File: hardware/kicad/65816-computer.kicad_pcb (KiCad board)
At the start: 4 copper layers, 169.5 x 99.7 mm, 61 parts, among them J1 Ext_Pwr_Led, J2 Ext_Sw_Res, J3 Power, J4 UART_A, J5 UART_B, J6 Port_A, J7 Port_B, SW1 SW_Res, U1 74AC04, U11 74AC138, U12 SC16C752, U13 W65C22S, U2 74AC245, U3 74AC573, U4 W65C816S, U5 DS1813-5+, U6 Address_Decoder, U7 AS6C4008, U8 AS6C4008, U9 AT28C256, X1 MXO45HS

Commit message: update schematic, add draft PCB
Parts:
- removed the REF** at (-217.2, 150.5)
- removed the REF** at (-148.0, 147.3)
- removed the REF** at (-155.6, 231.8)
- removed the REF** at (-194.3, 231.8)
- removed the REF** at (-170.8, 238.8)
- removed the REF** at (-155.6, 238.8)
- removed the REF** at (-215.9, 226.1)
- removed the REF** at (-147.3, 238.1)
- removed the REF** at (-292.1, 203.2)
- removed the REF** at (-158.1, 238.8)
- removed the REF** at (-308.6, 238.1)
- removed the REF** at (-165.7, 238.8)
- removed the REF** at (-163.2, 238.8)
- removed the REF** at (-173.4, 239.0)
- removed the REF** at (-308.6, 147.3)
- removed the REF** at (-155.6, 234.3)
- removed the REF** at (-168.3, 238.8)
- removed the REF** at (-160.7, 238.8)
- added C13: 0.1 µF, Capacitor_SMD:C_0603_1608Metric_Pad1.08x0.95mm_HandSolder, F.Cu at (147.3, 97.2)
- added C14: 0.1 µF, Capacitor_SMD:C_0603_1608Metric_Pad1.08x0.95mm_HandSolder, F.Cu at (170.8, 62.5)
- added C15: C_Polarized, Capacitor_THT:CP_Radial_D6.3mm_P2.50mm, F.Cu at (126.1, 45.0)
- added H1: MountingHole_Pad, MountingHole:MountingHole_3.2mm_M3_Pad_Via, F.Cu at (73.5, 44.8)
- added H2: MountingHole_Pad, MountingHole:MountingHole_3.2mm_M3_Pad_Via, F.Cu at (232.8, 45.0)
- added H3: MountingHole_Pad, MountingHole:MountingHole_3.2mm_M3_Pad_Via, F.Cu at (73.5, 134.2)
- added H4: MountingHole_Pad, MountingHole:MountingHole_3.2mm_M3_Pad_Via, F.Cu at (232.9, 134.4)
- added J10: Conn_01x08, Connector_PinHeader_2.54mm:PinHeader_1x08_P2.54mm_Vertical, F.Cu at (201.9, 126.7)
- added J11: Conn_01x04, Connector_PinHeader_2.54mm:PinHeader_1x04_P2.54mm_Vertical, F.Cu at (146.1, 44.5)
- added J12: Conn_01x08, Connector_PinHeader_2.54mm:PinHeader_1x08_P2.54mm_Vertical, F.Cu at (80.8, 87.9)
- added J8: Conn_01x08, Connector_PinHeader_2.54mm:PinHeader_1x08_P2.54mm_Vertical, F.Cu at (201.9, 133.6)
- added J9: Conn_01x08, Connector_PinHeader_2.54mm:PinHeader_1x08_P2.54mm_Vertical, F.Cu at (227.1, 133.6)
- added JP2: CLK_SEL, Connector_PinHeader_2.54mm:PinHeader_1x03_P2.54mm_Vertical, F.Cu at (115.0, 44.5)
- added JP3: Jumper_2_Bridged, Connector_PinHeader_2.54mm:PinHeader_1x02_P2.54mm_Vertical, F.Cu at (112.0, 70.6)
- added R10: 10 k, Resistor_SMD:R_0603_1608Metric_Pad0.98x0.95mm_HandSolder, F.Cu at (219.5, 127.5)
- added R11: 10 k, Resistor_SMD:R_0603_1608Metric_Pad0.98x0.95mm_HandSolder, F.Cu at (216.9, 127.5)
- added R12: 10 k, Resistor_SMD:R_0603_1608Metric_Pad0.98x0.95mm_HandSolder, F.Cu at (214.4, 127.5)
- added R13: 10 k, Resistor_SMD:R_0603_1608Metric_Pad0.98x0.95mm_HandSolder, F.Cu at (211.8, 127.5)
- added R14: 10 k, Resistor_SMD:R_0603_1608Metric_Pad0.98x0.95mm_HandSolder, F.Cu at (209.3, 127.5)
- added R15: 10 k, Resistor_SMD:R_0603_1608Metric_Pad0.98x0.95mm_HandSolder, F.Cu at (188.6, 81.3)
- added R16: 10 k, Resistor_SMD:R_0603_1608Metric_Pad0.98x0.95mm_HandSolder, F.Cu at (186.7, 81.3)
- added R7: 10 k, Resistor_SMD:R_0603_1608Metric_Pad0.98x0.95mm_HandSolder, F.Cu at (227.1, 127.5)
- added R8: 10 k, Resistor_SMD:R_0603_1608Metric_Pad0.98x0.95mm_HandSolder, F.Cu at (224.5, 127.5)
- added R9: 10 k, Resistor_SMD:R_0603_1608Metric_Pad0.98x0.95mm_HandSolder, F.Cu at (222.0, 127.5)
- added REF**: Oscillator_SMD_IDT_JU6-6_7.0x5.0mm_P2.54mm, Oscillator:Oscillator_SMD_IDT_JU6-6_7.0x5.0mm_P2.54mm, F.Cu at (93.5, 60.9)
- added SW2: SW_DIP_x02, Button_Switch_SMD:SW_DIP_SPSTx02_Slide_6.7x6.64mm_W8.61mm_P2.54mm_LowProfile, F.Cu at (185.4, 90.9)
- added TP1: CLK, TestPoint:TestPoint_Keystone_5005-5009_Compact, F.Cu at (119.4, 72.4)
- added TP10: GND, TestPoint:TestPoint_Keystone_5005-5009_Compact, F.Cu at (182.2, 79.4)
- added TP11: X1_OUT, TestPoint:TestPoint_Keystone_5005-5009_Compact, F.Cu at (123.7, 51.1)
- added TP2: X2_OUT, TestPoint:TestPoint_Keystone_5005-5009_Compact, F.Cu at (117.6, 51.1)
- added TP3: RES, TestPoint:TestPoint_Pad_D1.5mm, F.Cu at (83.3, 118.9)
- added TP4: ~{RES}, TestPoint:TestPoint_Keystone_5005-5009_Compact, F.Cu at (113.0, 99.1)
- added TP7: GND, TestPoint:TestPoint_Keystone_5005-5009_Compact, F.Cu at (124.5, 72.4)
- added TP8: GND, TestPoint:TestPoint_Keystone_5005-5009_Compact, F.Cu at (184.8, 111.8)
- added TP9: GND, TestPoint:TestPoint_Keystone_5005-5009_Compact, F.Cu at (118.1, 99.3)
- added U10: 74AC74, Package_DIP:DIP-14_W7.62mm_Socket, F.Cu at (105.4, 64.6)
- added X2: MXO45HS, Oscillator:Oscillator_DIP-8, F.Cu at (73.8, 64.8)
- J1: value Ext_Pwr_Led -> EXT_LED_PWR
- J2: value Ext_Sw_Res -> EXT_SW_RES
- J3: footprint Connector_PinHeader_2.54mm:PinHeader_1x02_P2.54mm_Vertical -> Connector_JST:JST_XH_B2B-XH-A_1x02_P2.50mm_Vertical
- R4, R5, R6: value 1k -> 1 k
- SW1: value SW_Res -> SW_RES
- U1: value 74AC04 -> SST39LF010; footprint Package_DIP:DIP-14_W7.62mm_Socket -> Package_LCC:PLCC-32_11.4x14.0mm_P1.27mm
- U5: value DS1813-5+ -> MIC2775; footprint Package_TO_SOT_THT:TO-92 -> Package_TO_SOT_SMD:SOT-23-5_HandSoldering
- moved C5 534.0 mm to (176.8, 122.4), turned to 180 degrees
- moved R6 517.0 mm to (105.9, 47.9), turned to 180 degrees
- moved R3 494.2 mm to (137.2, 97.2), turned to -90 degrees
- moved C4 493.8 mm to (139.7, 51.7), turned to 180 degrees
- moved C3 493.3 mm to (139.7, 64.5), turned to 180 degrees
- moved C9 475.4 mm to (195.0, 102.1)
- moved U1 463.8 mm to (184.2, 62.9), turned to 90 degrees
- moved R2 436.7 mm to (132.1, 97.2), turned to -90 degrees
- moved C8 412.9 mm to (93.7, 125.5), turned to -90 degrees
- moved C10 406.2 mm to (190.5, 81.3), turned to -90 degrees
- moved X1 404.3 mm to (89.7, 64.6)
- moved J3 399.2 mm to (84.6, 46.0)
- moved C2 398.5 mm to (200.6, 51.8)
- moved C6 397.0 mm to (72.9, 53.1), turned to 180 degrees
- moved C7 396.7 mm to (79.5, 71.6)
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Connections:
- J2 pad 1: /CPU& Bank Address Latching/~{RES} -> /CPU& Bank Address Latching/~{RES_BTN}
- J4 pad 8: /IO/UART_TXA -> /IO/UART_RXA
- SW1 pad 1: /CPU& Bank Address Latching/~{RES} -> GND
- SW1 pad 2: GND -> /CPU& Bank Address Latching/~{RES_BTN}
- U1 pad 1: /CPU& Bank Address Latching/CLK -> GND
- U1 pad 10: unconnected-(U1-Pad10) -> /CPU& Bank Address Latching/A2
- U1 pad 11: GND -> /CPU& Bank Address Latching/A1
- U1 pad 12: unconnected-(U1-Pad12) -> /CPU& Bank Address Latching/A0
- U1 pad 13: GND -> /CPU& Bank Address Latching/D0
- U1 pad 14: +5V -> /CPU& Bank Address Latching/D1
- U1 pad 2: /CPU& Bank Address Latching/CLK_INV -> GND
- U1 pad 3: /CPU& Bank Address Latching/~{RES} -> GND
- U1 pad 4: /CPU& Bank Address Latching/RES -> /CPU& Bank Address Latching/A12
- U1 pad 5: GND -> /CPU& Bank Address Latching/A7
- U1 pad 6: unconnected-(U1-Pad6) -> /CPU& Bank Address Latching/A6
- U1 pad 7: GND -> /CPU& Bank Address Latching/A5
- U1 pad 8: unconnected-(U1-Pad8) -> /CPU& Bank Address Latching/A4
- U1 pad 9: GND -> /CPU& Bank Address Latching/A3
- U11 pad 10: unconnected-(U11-Pad10) -> /IO/~{IO5}
- U11 pad 11: unconnected-(U11-Pad11) -> /IO/~{IO4}
- U11 pad 12: unconnected-(U11-Pad12) -> /IO/~{IO3}
- U11 pad 7: unconnected-(U11-Pad7) -> /IO/~{IO7}
- U11 pad 9: unconnected-(U11-Pad9) -> /IO/~{IO6}
- U12 pad 13: /CPU& Bank Address Latching/CLK -> /CPU& Bank Address Latching/CLK_UART
- U12 pad 17: unconnected-(U12-Pad17) -> GND
- U12 pad 42: unconnected-(U12-Pad42) -> +5V
- U12 pad 5: /IO/UART_TXA -> /IO/UART_RXA
- U13 pad 23: /IO/~{IOCS} -> /IO/~{IO0}
- U4 pad 39: unconnected-(U4-Pad39) -> /CPU& Bank Address Latching/VDA
- U4 pad 7: unconnected-(U4-Pad7) -> /CPU& Bank Address Latching/VPA
- U5 pad 2: +5V -> GND
- U5 pad 3: GND -> /CPU& Bank Address Latching/RES
- U6 pad 13: unconnected-(U6-Pad13) -> Net-(U6-Pad13)
- U6 pad 3: unconnected-(U6-Pad3) -> /CPU& Bank Address Latching/VPA
- U6 pad 4: unconnected-(U6-Pad4) -> /CPU& Bank Address Latching/VDA
- U9 pad 1: GND -> /Memory/ROMSW1
- U9 pad 26: GND -> /Memory/ROMSW0
- X1 pad 1: unconnected-(X1-Pad1) -> +5V
- X1 pad 5: /CPU& Bank Address Latching/CLK -> /CPU& Bank Address Latching/CLK_UART
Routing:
- net /CPU& Bank Address Latching/A0: track 51.9 -> 354.6 mm, vias 0 -> 2
- net /CPU& Bank Address Latching/A1: track 51.6 -> 347.6 mm, vias 0 -> 2
- net /CPU& Bank Address Latching/A2: track 51.8 -> 342.4 mm, vias 0 -> 2
- net /CPU& Bank Address Latching/A18: track 25.8 -> 302.0 mm
- net /Memory/~{RAM1CS}: track 0.00 -> 272.6 mm, vias 0 -> 3
- net /CPU& Bank Address Latching/A17: track 25.7 -> 283.8 mm
- net /CPU& Bank Address Latching/A16: track 25.9 -> 283.1 mm
- net /CPU& Bank Address Latching/RES: track 0.00 -> 257.0 mm, vias 0 -> 3
- net /CPU& Bank Address Latching/A10: track 51.5 -> 301.1 mm, vias 0 -> 1
- net /Memory/~{RD}: track 51.6 -> 288.3 mm, vias 0 -> 1
- net /CPU& Bank Address Latching/A11: track 51.6 -> 286.0 mm, vias 0 -> 1
- net /CPU& Bank Address Latching/A9: track 51.5 -> 264.6 mm, vias 0 -> 1
- net /CPU& Bank Address Latching/A12: track 51.5 -> 258.8 mm, vias 0 -> 1
- net /Memory/~{WR}: track 25.8 -> 226.0 mm, vias 0 -> 1
- net /CPU& Bank Address Latching/D4: track 158.7 -> 357.9 mm, vias 0 -> 1
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- added copper zone on In1.Cu, net +5V
- added copper zone on In2.Cu, net GND
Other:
- board size 169.5 x 99.7 mm -> 169.7 x 99.8 mm
- board text added: "(c) 2022 Michael Billington"
- board text added: "A0"
- board text added: "A1"
- board text added: "A10"
- board text added: "A11"
- board text added: "A12"
- board text added: "A13"
- board text added: "A14"
- board text added: "A15"
- board text added: "A16"
- board text added: "A17"
- board text added: "A18"
- board text added: "A19"
- board text added: "A2"
- board text added: "A3"
- board text added: "A4"
- board text added: "A5"
- board text added: "A6"
- board text added: "A7"
- board text added: "A8"
- board text added: "A9"
- board text added: "D0"
- board text added: "D1"
- board text added: "D2"
- board text added: "D3"
- board text added: "D4"
- board text added: "D5"
- board text added: "D6"
- board text added: "D7"
- board text added: "GND"
- board text added: "OUT"
- board text added: "PWR"
- board text added: "RES"
- board text added: "RESET"
- board text added: "X1"
- board text added: "X2"
- board text added: "~{CE}"
- board text added: "~{OE}"
- board text added: "~{WE}"

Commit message: pcb updates
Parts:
- added C16: 4.7 µF, Capacitor_THT:CP_Radial_D4.0mm_P1.50mm, F.Cu at (130.7, 125.9)
- added D3: EMU, LED_SMD:LED_0603_1608Metric_Pad1.05x0.95mm_HandSolder, F.Cu at (163.1, 42.9)
- added J13: Conn_01x06, Connector_PinHeader_2.54mm:PinHeader_1x06_P2.54mm_Vertical, F.Cu at (135.1, 69.3)
- added J14: Conn_01x06, Connector_PinHeader_2.54mm:PinHeader_1x06_P2.54mm_Vertical, F.Cu at (117.2, 93.3)
- added J15: Conn_01x02, Connector_PinHeader_2.54mm:PinHeader_1x02_P2.54mm_Vertical, F.Cu at (79.5, 135.4)
- added J16: Conn_01x06, Connector_PinHeader_2.54mm:PinHeader_1x06_P2.54mm_Vertical, F.Cu at (98.3, 72.1)
- added J17: Conn_01x04, Connector_PinHeader_2.54mm:PinHeader_1x04_P2.54mm_Vertical, F.Cu at (80.8, 71.9)
- added J18: Conn_01x07, Connector_PinSocket_2.54mm:PinSocket_1x07_P2.54mm_Vertical, F.Cu at (111.5, 126.0)
- added J19: Conn_02x06, Connector_PinHeader_2.54mm:PinHeader_2x03_P2.54mm_Vertical, F.Cu at (132.2, 135.0)
- added J20: Conn_01x02, Connector_PinHeader_2.54mm:PinHeader_1x02_P2.54mm_Vertical, F.Cu at (187.3, 119.1)
- added JP4: Jumper_2_Bridged, Connector_PinHeader_2.54mm:PinHeader_1x02_P2.54mm_Vertical, F.Cu at (106.8, 92.4)
- added JP5: SolderJumper_2_Open, Jumper:SolderJumper-2_P1.3mm_Open_RoundedPad1.0x1.5mm, F.Cu at (140.1, 44.3)
- added R17: 1 k, Resistor_SMD:R_0603_1608Metric_Pad0.98x0.95mm_HandSolder, F.Cu at (167.8, 42.9)
- added TP5: ~{IRQ}, TestPoint:TestPoint_Keystone_5005-5009_Compact, F.Cu at (108.2, 99.1)
- added TP6: ~{NMI}, TestPoint:TestPoint_Keystone_5005-5009_Compact, F.Cu at (183.1, 104.5)
- added U14: DS1813-5+, Package_TO_SOT_THT:TO-92_Inline, F.Cu at (133.2, 44.6)
- added X2_ALT: Oscillator_SMD_IDT_JU6-6_7.0x5.0mm_P2.54mm, Oscillator:Oscillator_SMD_IDT_JU6-6_7.0x5.0mm_P2.54mm, F.Cu at (77.6, 61.0)
- C15: value C_Polarized -> 100 µF
- U13, U4: footprint Package_DIP:DIP-40_W15.24mm -> Package_DIP:DIP-40_W15.24mm_Socket
- moved R3 22.4 mm to (122.0, 80.6), turned to 0 degrees
- moved J4 19.2 mm to (101.6, 132.8), turned to -90 degrees
- moved R1 17.0 mm to (122.0, 85.7), turned to 0 degrees
- moved J7 16.4 mm to (162.2, 134.9)
- moved J6 16.4 mm to (142.4, 134.9)
- moved R2 11.9 mm to (122.0, 90.8), turned to 0 degrees
- moved JP1 9.71 mm to (125.7, 119.5)
- moved TP3 8.29 mm to (87.1, 126.2)
- moved TP8 8.18 mm to (188.3, 104.4)
- moved C7 6.53 mm to (75.4, 76.7), turned to -90 degrees
- moved LS1 5.77 mm to (118.2, 111.9), turned to 180 degrees
- moved JP2 5.06 mm to (120.0, 44.5), turned to -90 degrees
- moved TP2 3.72 mm to (113.9, 50.5)
- moved JP3 3.18 mm to (109.2, 72.1), turned to -90 degrees
- moved C5 1.73 mm to (178.1, 123.6), turned to -90 degrees
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- renumbered REF** to X1_ALT
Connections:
- net Net-(JP1-Pad2) renamed /IO/SPEAKER
- net Net-(U6-Pad13) renamed /Memory/S0
- U12 pad 29: unconnected-(U12-Pad29) -> /IO/UART_INTB
- U12 pad 30: unconnected-(U12-Pad30) -> /IO/UART_INTA
- U4 pad 1: unconnected-(U4-Pad1) -> /CPU& Bank Address Latching/~{VP}
- U4 pad 35: unconnected-(U4-Pad35) -> /CPU& Bank Address Latching/EMU
- U4 pad 38: unconnected-(U4-Pad38) -> /CPU& Bank Address Latching/MX
- U4 pad 4: +5V -> /CPU& Bank Address Latching/~{IRQ}
- U4 pad 5: unconnected-(U4-Pad5) -> /CPU& Bank Address Latching/~{ML}
- U6 pad 20: unconnected-(U6-Pad20) -> /Memory/S1
- U6 pad 21: unconnected-(U6-Pad21) -> /Memory/S2
- U6 pad 22: unconnected-(U6-Pad22) -> /Memory/S3
- U6 pad 23: unconnected-(U6-Pad23) -> /Memory/S4
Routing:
- net /CPU& Bank Address Latching/~{RES}: track 148.7 -> 225.5 mm, vias 3 -> 2
- net /CPU& Bank Address Latching/EMU: track 0.00 -> 63.0 mm
- net /CPU& Bank Address Latching/~{IRQ}: track 0.00 -> 44.5 mm
- net /IO/VIA_PB7: track 63.7 -> 104.7 mm, vias 1 -> 0
- net /IO/~{UART_TXRDYA}: track 17.0 -> 52.4 mm
- net /CPU& Bank Address Latching/~{NMI}: track 61.4 -> 93.5 mm, vias 2 -> 3
- net /IO/UART_INTA: track 0.00 -> 30.1 mm
- net /Memory/~{WR}: track 226.0 -> 256.0 mm
- net /CPU& Bank Address Latching/~{ML}: track 0.00 -> 29.5 mm
- net /IO/UART_INTB: track 0.00 -> 27.9 mm
- net /IO/VIA_PA0: track 16.3 -> 43.1 mm
- net /IO/VIA_PA1: track 12.3 -> 38.4 mm
- net /IO/~{UART_RIA}: track 16.8 -> 41.9 mm
- net /IO/VIA_PA2: track 15.8 -> 39.6 mm
- net /IO/~{UART_CDA}: track 14.2 -> 36.3 mm
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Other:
- board text added: "+"
- board text added: "1.8432 MHz"
- board text added: "65C816"
- board text added: "74AC138"
- board text added: "74AC245"
- board text added: "74AC573"
- board text added: "74AC74"
- board text added: "AS6C4008"
- board text added: "AT28C256"
- board text added: "ATF22V10 Address Decode"
- board text added: "BE"
- board text added: "CA1"
- board text added: "CA2"
- board text added: "CB1"
- board text added: "CB2"
- board text added: "CLK"
- board text added: "CPU"
- board text added: "CS1"
- board text added: "EMU"
- board text added: "INTA"
- board text added: "INTB"
- board text added: "MX"
- board text added: "NC"
- board text added: "PA0"
- board text added: "PA1"
- board text added: "PA2"
- board text added: "PA3"
- board text added: "PA4"
- board text added: "PA5"
- board text added: "PA6"
- board text added: "PA7"
- board text added: "PB0"
- board text added: "PB1"
- board text added: "PB2"
- board text added: "PB3"
- board text added: "PB4"
- board text added: "PB5"
- board text added: "PB6"
- board text added: "PB7"
- board text added: "RAM0"
- board text added: "RAM1"
- board text added: "ROM"
- board text added: "ROM_BANK"
- board text added: "RX"
- board text added: "R~{W}"
- board text added: "S0"
- board text added: "S1"
- board text added: "S2"
- board text added: "S3"
- board text added: "S4"
- board text added: "SEL"
- board text added: "SPEAKER"
- board text added: "SST39LF010 ROM"
- board text added: "TX"
- board text added: "T~{R}"
- board text added: "U14_ENABLE"
- board text added: "VCC"
- board text added: "VDA"
- board text added: "VIA"
- board text added: "WDC 65C22S"
- board text added: "WDC 65C816S"
- board text added: "microSD module DEV-13743"
- board text added: "~{ABORT}"
- board text added: "~{CD}"
- board text added: "~{CS2}"
- board text added: "~{CTS}"
- board text added: "~{DSR}"
- board text added: "~{DTR}"
- board text added: "~{IO0}"
- board text added: "~{IO1}"
- board text added: "~{IO2}"
- board text added: "~{IO3}"
- board text added: "~{IO4}"
- board text added: "~{IO5}"
- board text added: "~{IO6}"
- board text added: "~{IO7}"
- board text added: "~{IO}"
- board text added: "~{IRQ}"
- board text added: "~{LE}"
- board text added: "~{ML}"
- board text added: "~{NMI}"
- board text added: "~{OP}"
- board text added: "~{RAM0}"
- board text added: "~{RAM1}"
- board text added: "~{RDY}"
- board text added: "~{RD}"
- board text added: "~{RES}"
- board text added: "~{RI}"
- board text added: "~{ROM}"
- board text added: "~{RTS}"
- board text added: "~{RW}"
- board text added: "~{RXRDY}"
- board text added: "~{TXRDY}"
- board text added: "~{VP}"
- board text added: "~{WR}"
- board text added: "© 2022 Michael Billington"
- board text removed: "(c) 2022 Michael Billington"
- board text removed: "OUT"

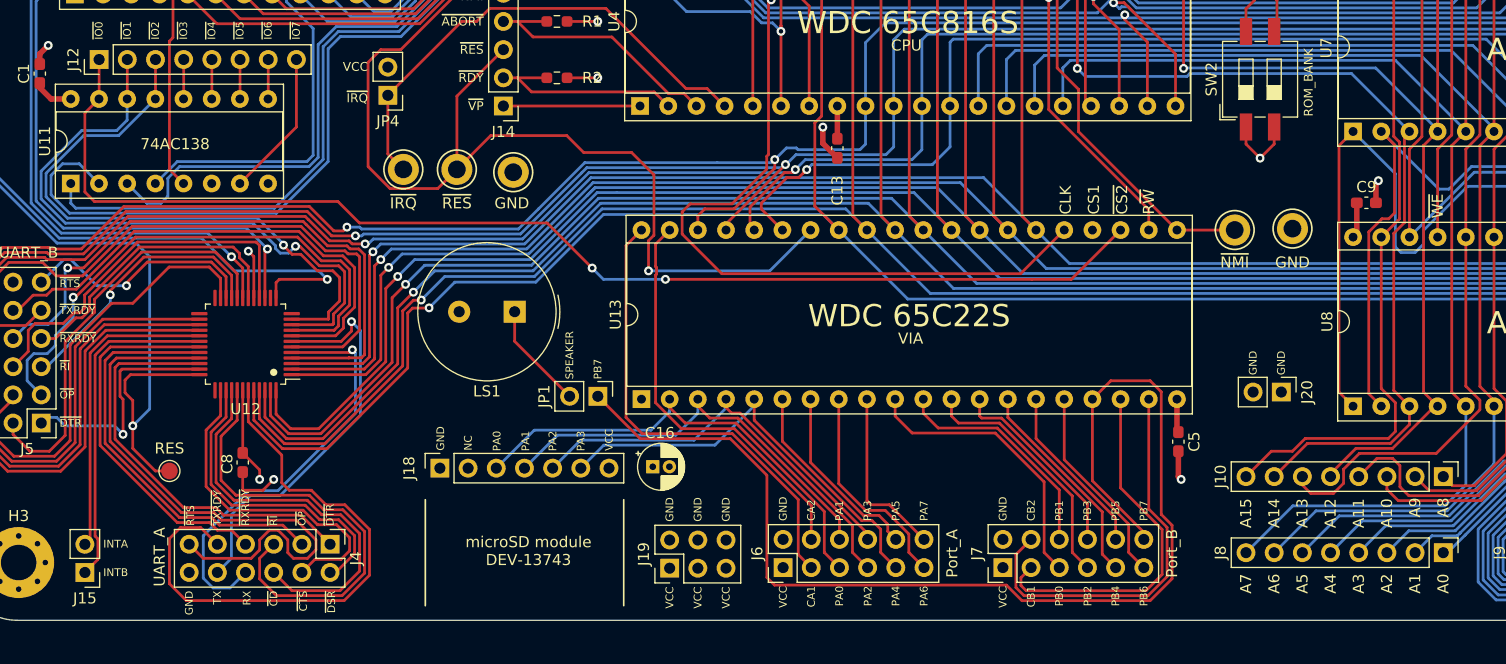
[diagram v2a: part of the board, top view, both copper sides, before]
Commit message: add gerbers for test board
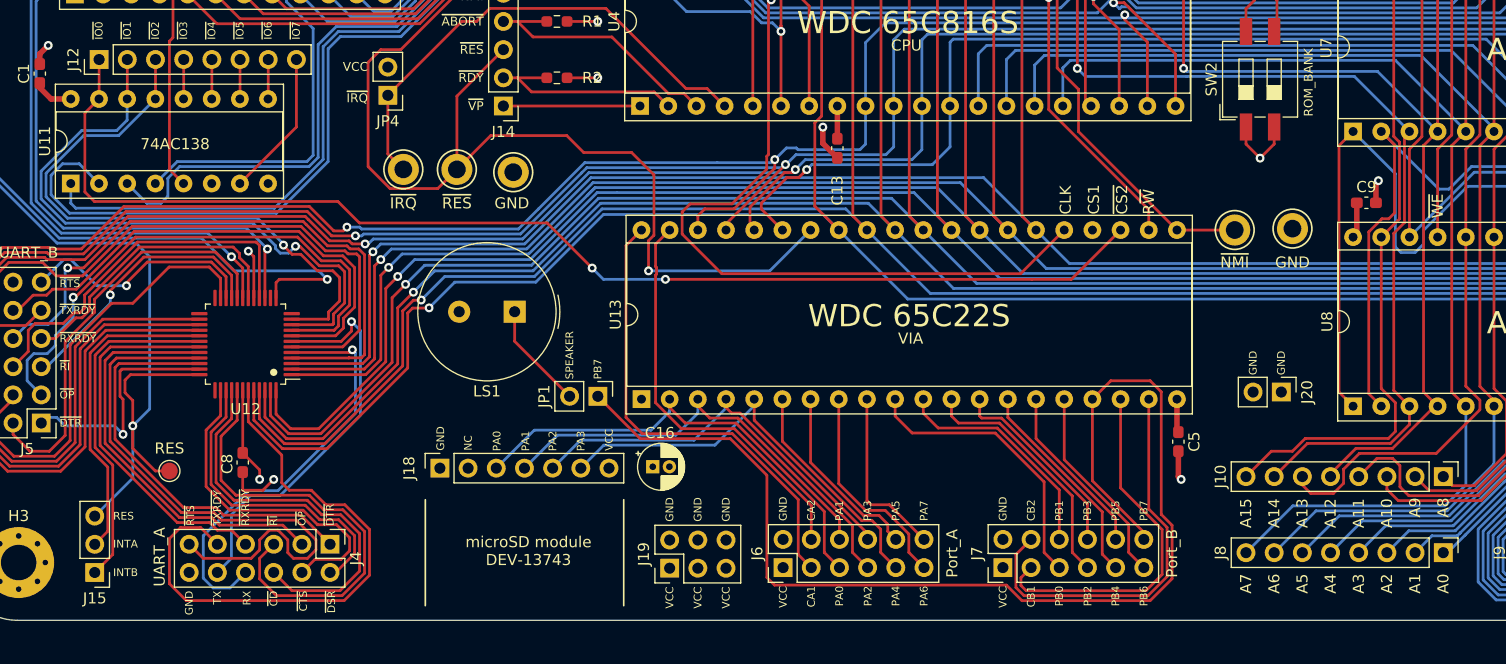
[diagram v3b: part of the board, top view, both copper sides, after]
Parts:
- J15: value Conn_01x02 -> Conn_01x03; footprint Connector_PinHeader_2.54mm:PinHeader_1x02_P2.54mm_Vertical -> Connector_PinHeader_2.54mm:PinHeader_1x03_P2.54mm_Vertical
- moved J15 0.89 mm to (80.4, 135.4)
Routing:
- net /CPU& Bank Address Latching/RES: track 263.9 -> 273.5 mm
- net /IO/UART_INTB: track 27.9 -> 28.9 mm
- net /IO/UART_INTA: track 30.1 -> 30.8 mm
